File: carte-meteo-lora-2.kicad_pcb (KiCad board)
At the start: 4 copper layers, 80 parts, among them J1 USB_C_Receptacle_USB2.0_14P, J2 Conn_Coaxial, J3 Conn_Coaxial, J4 Conn_Coaxial, J5 Conn_01x04_Pin, SW1 SW_Push, SW2 SW_Push, U1 HS96L03W2C03, U2 SX1262TR8-GC, U3 LDL212PV33R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

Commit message: pcb: initial sectioning
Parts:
- moved C2 83.5 mm to (26.4, 116.4)
- moved U2 66.7 mm to (116.2, 164.0)
- moved C7 66.6 mm to (86.3, 69.9), turned to 180 degrees
- moved Y1 59.8 mm to (111.8, 81.8), turned to 90 degrees
- moved U4 59.6 mm to (96.3, 78.3), turned to 90 degrees
- moved TP9 59.6 mm to (67.0, 79.1), turned to 180 degrees
- moved C4 59.3 mm to (86.3, 71.8), turned to 180 degrees
- moved C8 58.7 mm to (86.3, 67.9), turned to 180 degrees
- moved R4 56.6 mm to (64.0, 160.5), turned to -90 degrees
- moved C3 55.7 mm to (86.3, 73.8), turned to 180 degrees
- moved TP8 55.4 mm to (67.0, 82.8), turned to 180 degrees
- moved J3 53.8 mm to (73.7, 79.5), turned to 180 degrees
- moved L2 53.5 mm to (83.4, 71.8), turned to 180 degrees
- moved R10 52.9 mm to (105.0, 79.4), turned to 90 degrees
- moved J2 52.9 mm to (83.1, 79.5), turned to 180 degrees
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
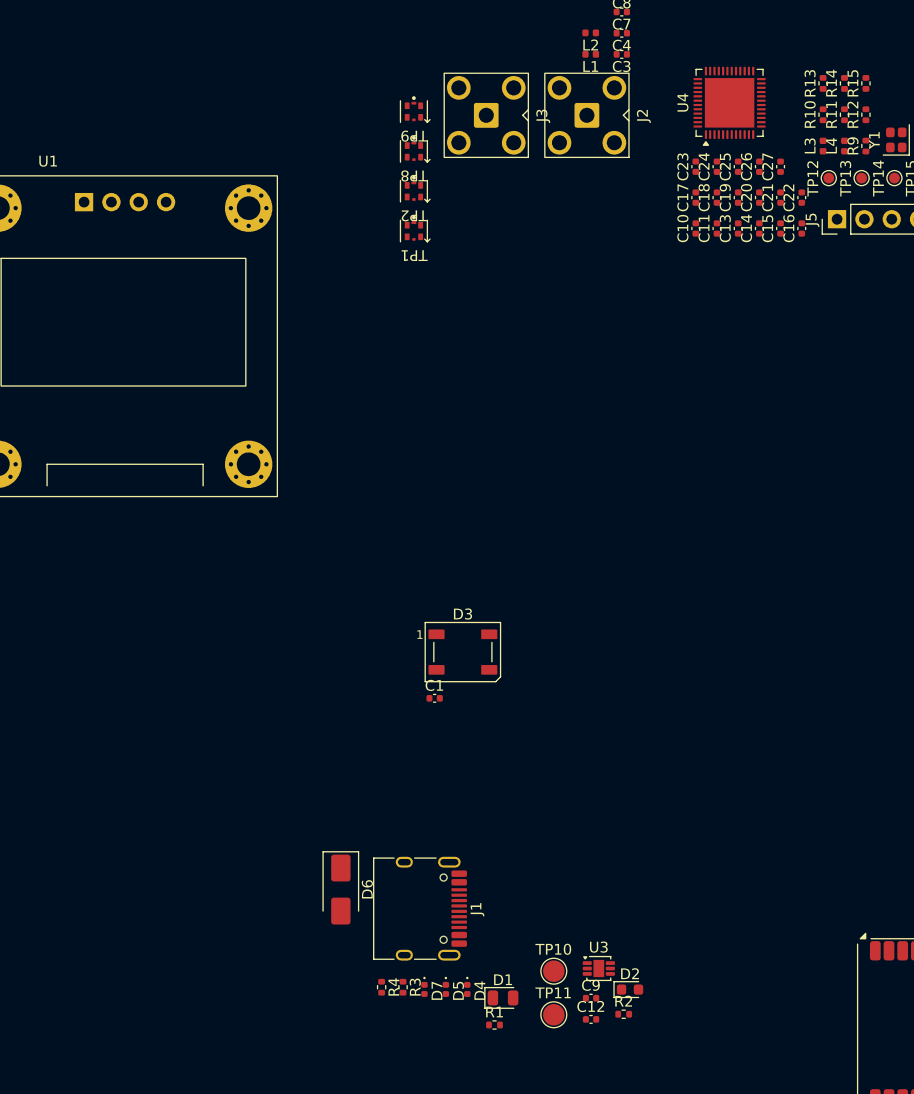
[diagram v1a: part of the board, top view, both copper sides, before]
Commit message: pcb: add usb inital layout
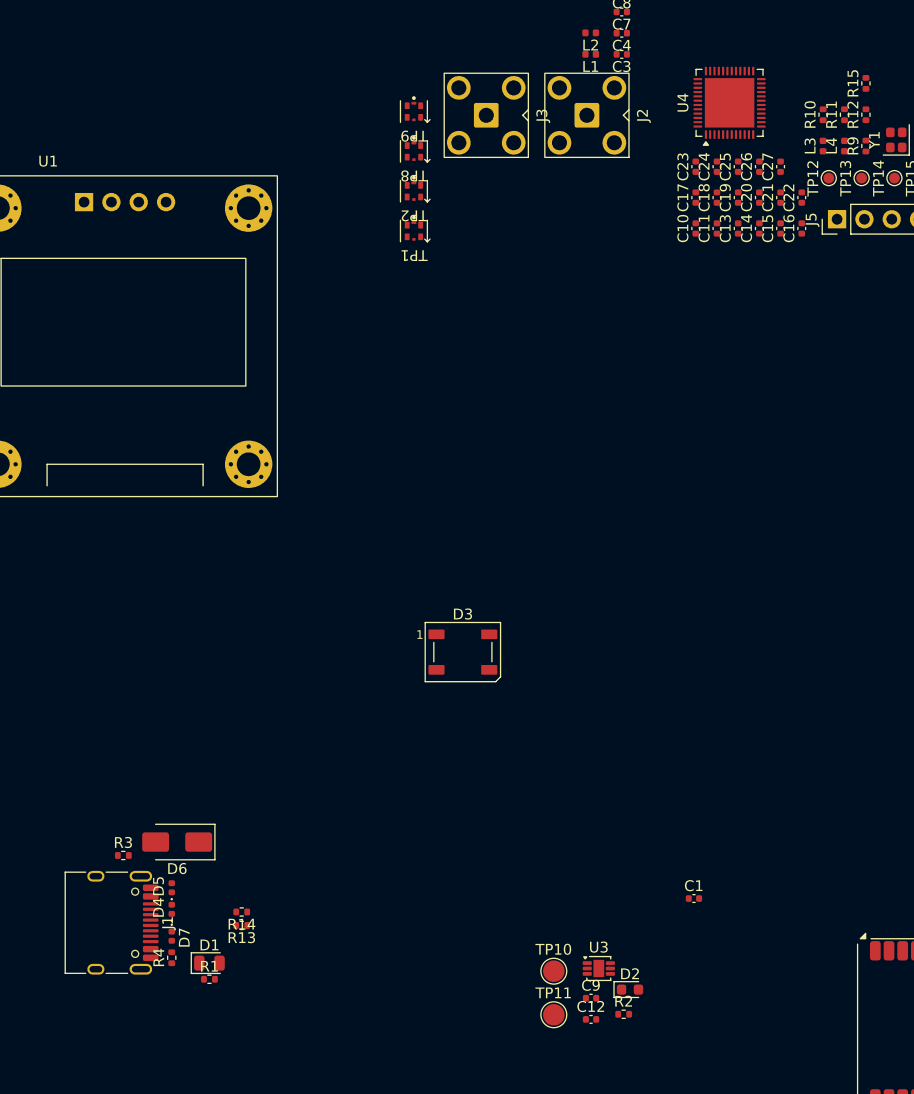
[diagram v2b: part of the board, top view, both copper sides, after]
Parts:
- moved R14 95.2 mm to (51.0, 153.5), turned to 180 degrees
- moved R13 95.1 mm to (51.0, 154.8), turned to 180 degrees
- moved C1 30.4 mm to (93.0, 152.2)
- moved R3 28.7 mm to (40.0, 148.2), turned to 0 degrees
- moved J1 28.7 mm to (38.5, 154.5)
- moved D4 28.5 mm to (44.5, 153.2), turned to 90 degrees
- moved D1 27.5 mm to (48.0, 158.2)
- moved D5 27.2 mm to (44.5, 151.2), turned to 90 degrees
- moved R1 26.8 mm to (48.0, 159.8)
- moved D7 24.0 mm to (44.5, 155.8)
- moved R4 19.7 mm to (44.5, 157.8), turned to 90 degrees
- moved D6 15.8 mm to (45.0, 147.0), turned to 180 degrees

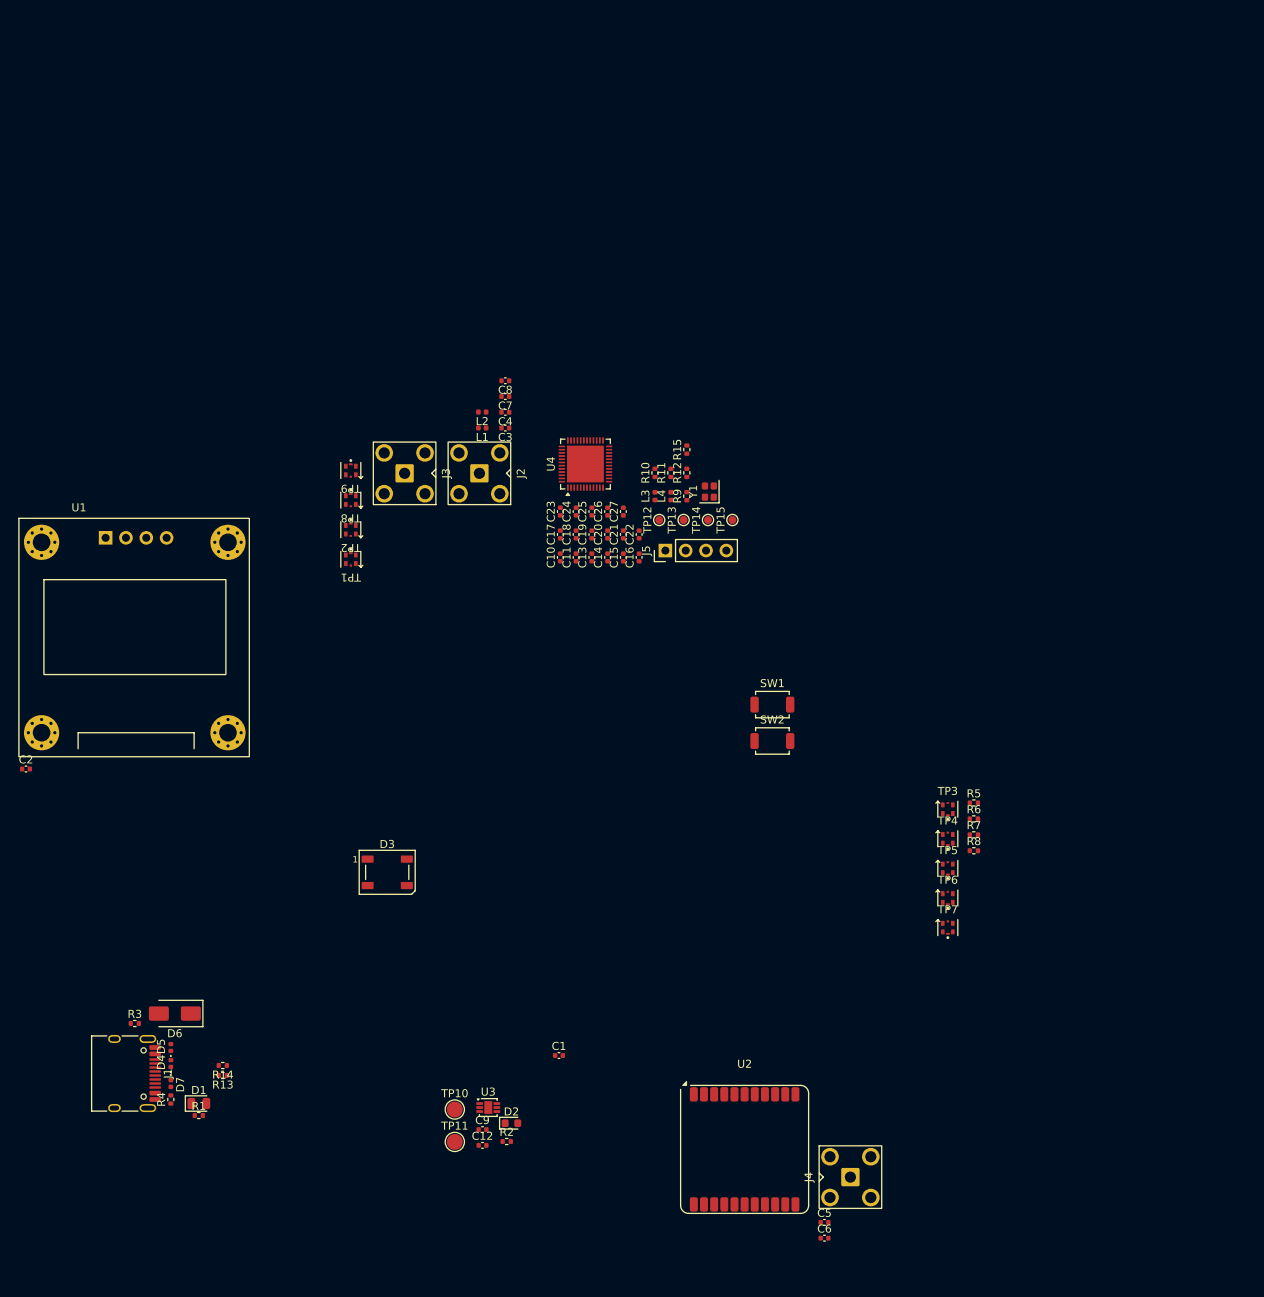
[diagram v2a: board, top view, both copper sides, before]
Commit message: pcb: add initial rf layout
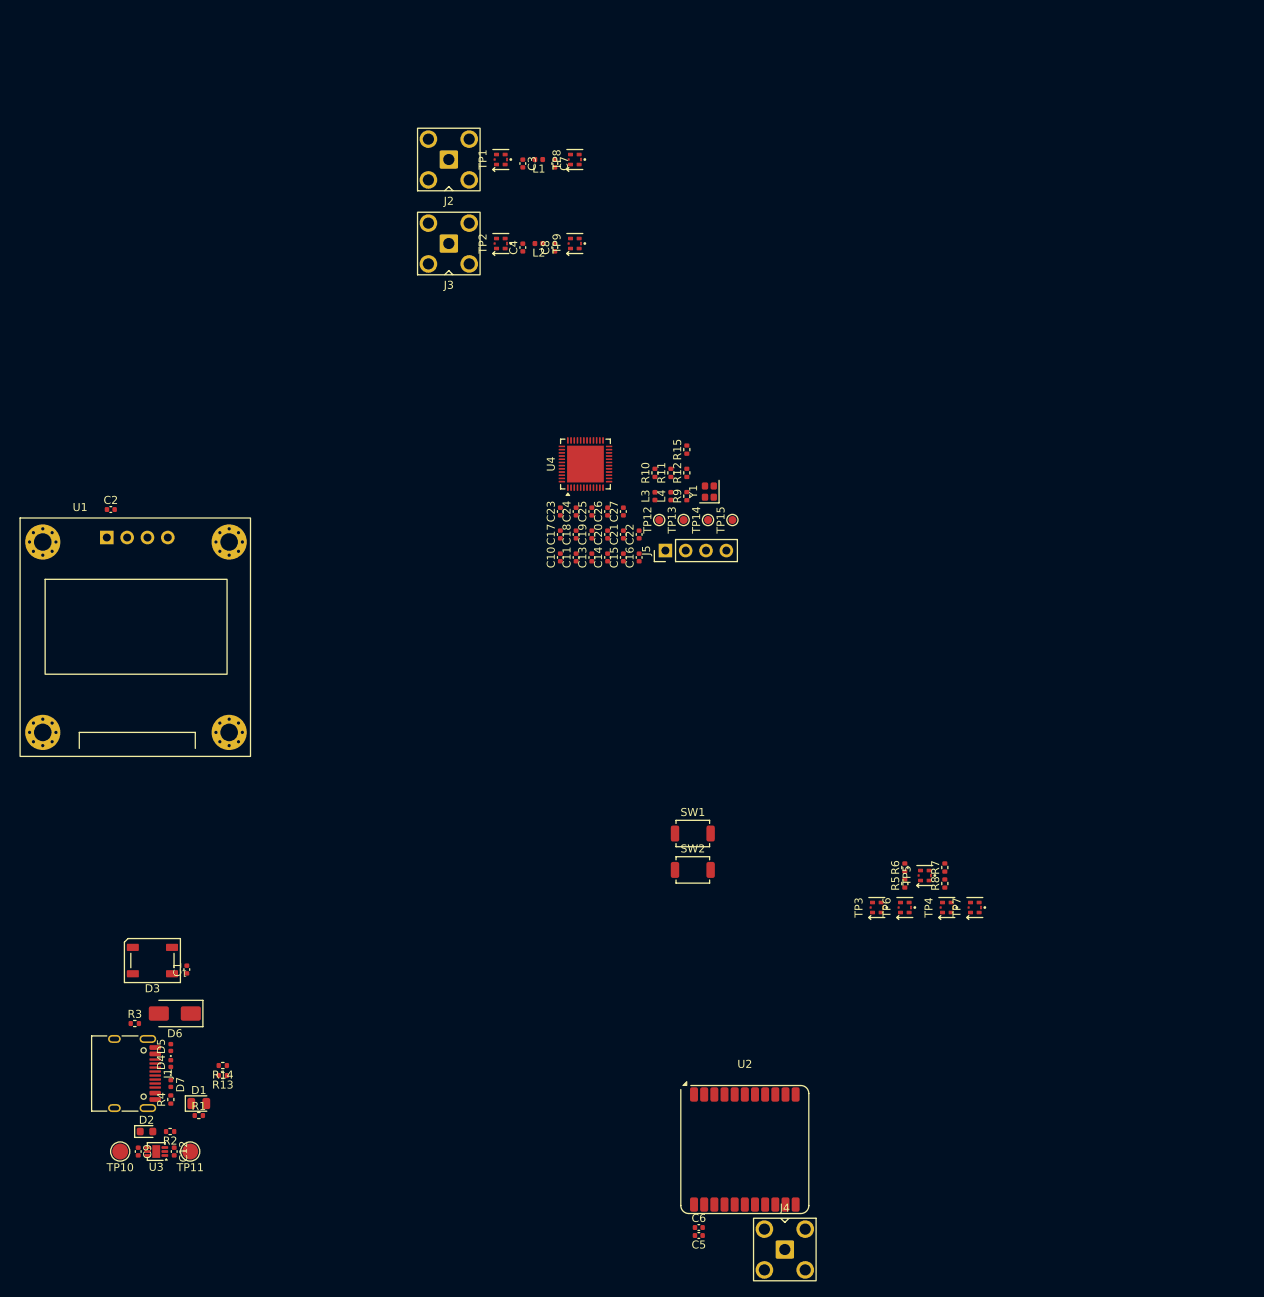
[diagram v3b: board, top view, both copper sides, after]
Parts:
- moved TP1 53.4 mm to (85.8, 40.2), turned to 90 degrees
- moved TP8 51.0 mm to (95.0, 40.2), turned to 90 degrees
- moved C1 47.7 mm to (46.5, 141.5), turned to 90 degrees
- moved D2 45.6 mm to (41.5, 161.8)
- moved C9 43.1 mm to (40.4, 164.2), turned to -90 degrees
- moved TP10 42.2 mm to (38.2, 164.2), turned to 180 degrees
- moved R2 42.1 mm to (44.4, 161.8), turned to 180 degrees
- moved U3 41.9 mm to (42.7, 164.2), turned to 180 degrees
- moved TP2 40.4 mm to (85.8, 50.8), turned to 90 degrees
- moved TP9 39.9 mm to (95.0, 50.8), turned to 90 degrees
- moved J2 39.4 mm to (79.2, 40.2), turned to 90 degrees
- moved C12 38.5 mm to (44.9, 164.2), turned to -90 degrees
- moved L1 34.3 mm to (90.5, 40.2)
- moved C2 34.1 mm to (37.0, 84.0)
- moved C3 33.1 mm to (88.5, 40.8), turned to -90 degrees
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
